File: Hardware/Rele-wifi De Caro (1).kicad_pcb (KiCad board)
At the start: 2 copper layers, 79.3 x 70.1 mm, 38 parts, among them IC1 MC7805CD2TG, J1 Screw_Terminal_01x03, J2 Screw_Terminal_01x03, J3 Screw_Terminal_01x03, J4 Screw_Terminal_01x03, J5 Screw_Terminal_01x02, K1 PR13-5V-450-1C, K2 PR13-5V-450-1C, K3 PR13-5V-450-1C, K4 PR13-5V-450-1C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

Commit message: PCB terminado
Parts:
- moved R3 1.60 mm to (160.3, 75.9)
- moved R2 1.57 mm to (160.2, 63.2)
- moved U2 1.53 mm to (144.0, 70.8)
- moved R1 1.49 mm to (160.2, 70.8)
- moved D1 1.41 mm to (160.2, 67.4), turned to 180 degrees
- moved Q7 0.48 mm to (166.3, 105.9)
- moved 10K4 0.48 mm to (171.1, 109.4)
- moved Q8 0.45 mm to (172.1, 104.4)
- moved IC1 0.44 mm to (140.0, 96.1)
- moved D8 0.43 mm to (171.8, 97.8)
- moved D7 0.40 mm to (161.3, 102.4)
- moved SW1 0.39 mm to (153.6, 96.2)
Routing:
- net VCC: track 177.9 -> 232.2 mm
- net Net-(IC1-VOUT): track 15.8 -> 29.9 mm
- net GPIO 16: track 65.6 -> 69.1 mm
- net Net-(D5-A): track 5.26 -> 6.86 mm
- net Net-(D2-A): track 12.6 -> 11.0 mm
- net Net-(D1-A): track 3.08 -> 4.28 mm
- net Net-(J5-Pin_2): track 16.4 -> 17.4 mm
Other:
- board size 79.3 x 70.1 mm -> 77 x 70.2 mm

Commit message: Add files via upload
PCB terminado
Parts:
- moved J5 56.6 mm to (134.9, 52.8), turned to 90 degrees
- moved SW1 49.1 mm to (145.6, 47.7), turned to 0 degrees
- moved IC1 33.1 mm to (139.6, 63.0)
- moved U2 25.7 mm to (144.0, 96.5)
- moved C5 22.4 mm to (142.1, 70.2)
- moved C6 19.8 mm to (147.8, 70.2), turned to 180 degrees
- moved R3 18.1 mm to (160.2, 94.0)
- moved R1 10.1 mm to (160.2, 80.9)
- moved R4 9.02 mm to (160.2, 99.0), turned to 0 degrees
- moved D5 1.84 mm to (161.2, 85.5), turned to -90 degrees
- moved D1 1.33 mm to (161.2, 68.3), turned to -90 degrees
- moved D7 1.07 mm to (161.2, 103.4), turned to 90 degrees
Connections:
- R1 pad 1: GPIO 15 -> GPIO 2
- R3 pad 1: GPIO 12 -> GPIO 14
- R4 pad 1: GPIO 16 -> GPIO 13
- U2 pad P$15: GPIO 16 -> unconnected-(U2-IO16-PadP$15)
- U2 pad P$3: GPIO 12 -> unconnected-(U2-IO12-PadP$3)
- U2 pad P$4: unconnected-(U2-IO13-PadP$4) -> GPIO 13
- U2 pad P$5: GPIO 15 -> unconnected-(U2-IO15-PadP$5)
- U2 pad P$6: unconnected-(U2-IO14-PadP$6) -> GPIO 14
- U2 pad P$7: unconnected-(U2-IO2-PadP$7) -> GPIO 2
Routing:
- net GPIO 16: track 69.1 -> 0.00 mm
- net VCC: track 232.2 -> 269.9 mm
- net GPIO 4: track 3.78 -> 28.2 mm
- net Net-(IC1-VOUT): track 29.9 -> 48.8 mm
- net GPIO 2: track 0.00 -> 13.5 mm
- net Net-(D1-A): track 4.28 -> 11.7 mm
- net Net-(J5-Pin_2): track 17.4 -> 10.7 mm
- net GPIO 12: track 3.88 -> 0.00 mm
- net GPIO 15: track 3.78 -> 0.00 mm
- net GPIO 13: track 0.00 -> 3.75 mm
- net GPIO 14: track 0.00 -> 3.74 mm
- net Net-(D7-K): track 3.77 -> 6.52 mm
- net Net-(D5-A): track 6.86 -> 7.48 mm
- net (no net): vias 0 -> 2
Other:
- board size 77 x 70.2 mm -> 76.2 x 70.2 mm

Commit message: PCB casi terminado
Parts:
- moved 10K4 0.55 mm to (170.6, 109.4)
- moved Q8 0.55 mm to (171.5, 104.4)
- moved Q7 0.46 mm to (165.8, 105.9)
- moved C5 0.45 mm to (142.5, 70.2), turned to 0 degrees
- moved D8 0.43 mm to (171.3, 97.8)
- moved Q5 0.07 mm to (166.2, 89.1)
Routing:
- net VCC: track 269.9 -> 254.4 mm
- net Net-(D8-A): track 18.0 -> 7.91 mm
- net Net-(D7-K): track 6.52 -> 0.00 mm
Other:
- board size 76.2 x 70.2 mm -> 76.2 x 70.3 mm

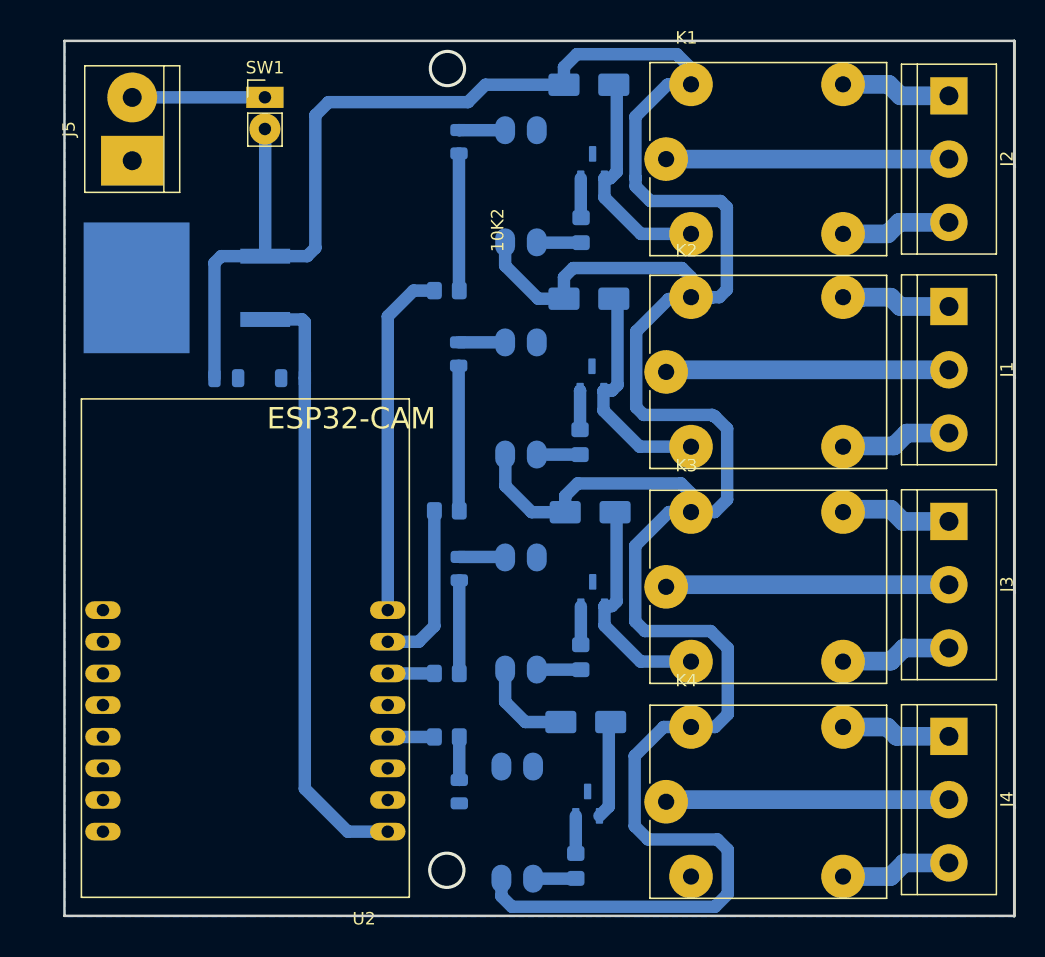
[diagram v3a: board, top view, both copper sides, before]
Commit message: PCB terminado y prolijo
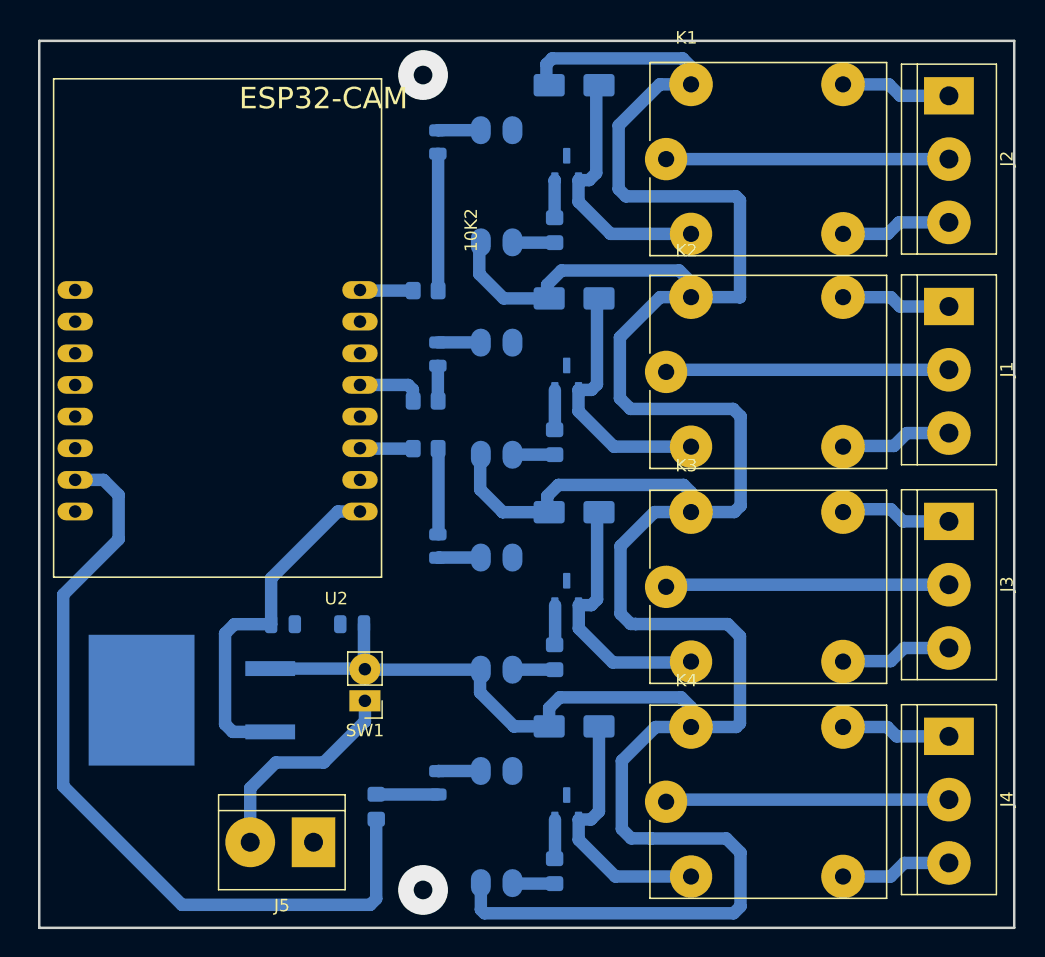
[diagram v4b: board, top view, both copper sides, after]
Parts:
- moved J5 56.6 mm to (149.5, 107.5), turned to 180 degrees
- moved SW1 49.1 mm to (153.6, 96.2), turned to 180 degrees
- moved IC1 33.1 mm to (140.0, 96.1)
- moved U2 25.8 mm to (141.8, 70.8)
- moved C5 22.2 mm to (152.6, 90.0), turned to 180 degrees
- moved C6 19.8 mm to (147.1, 90.0), turned to 0 degrees
- moved R3 18.1 mm to (158.5, 75.9)
- moved R1 8.98 mm to (158.5, 72.1)
- moved R4 7.97 mm to (154.5, 104.6), turned to 90 degrees
- moved D5 2.50 mm to (159.5, 83.7), turned to 90 degrees
- moved 10K2 2.12 mm to (168.8, 58.4)
- moved 10K3 2.10 mm to (168.8, 92.7)
- moved Q6 2.09 mm to (169.8, 87.5)
- moved Q3 2.09 mm to (169.8, 53.4)
- moved 10K1 2.04 mm to (168.8, 75.4)
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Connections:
- R1 pad 1: GPIO 2 -> GPIO 15
- R3 pad 1: GPIO 14 -> GPIO 12
- R4 pad 1: GPIO 13 -> GPIO 16
- U2 pad P$15: unconnected-(U2-IO16-PadP$15) -> GPIO 16
- U2 pad P$3: unconnected-(U2-IO12-PadP$3) -> GPIO 12
- U2 pad P$4: GPIO 13 -> unconnected-(U2-IO13-PadP$4)
- U2 pad P$5: unconnected-(U2-IO15-PadP$5) -> GPIO 15
- U2 pad P$6: GPIO 14 -> unconnected-(U2-IO14-PadP$6)
- U2 pad P$7: GPIO 2 -> unconnected-(U2-IO2-PadP$7)
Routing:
- net GPIO 16: track 0.00 -> 64.9 mm
- net GPIO 4: track 28.2 -> 4.27 mm
- net Net-(IC1-VOUT): track 48.8 -> 28.2 mm
- net GPIO 2: track 13.5 -> 0.00 mm
- net Net-(D8-A): track 7.91 -> 20.6 mm
- net Net-(D1-A): track 11.7 -> 2.83 mm
- net Net-(J5-Pin_2): track 10.7 -> 17.4 mm
- net GPIO 15: track 0.00 -> 5.31 mm
- net GPIO 12: track 0.00 -> 4.28 mm
- net VCC: track 254.4 -> 258.2 mm
- net GPIO 13: track 3.75 -> 0.00 mm
- net GPIO 14: track 3.74 -> 0.00 mm
- net Net-(D7-K): track 0.00 -> 3.42 mm
- net Net-(D6-A): track 18.0 -> 20.7 mm
- net Net-(D3-A): track 18.0 -> 20.5 mm
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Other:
- board size 76.2 x 70.3 mm -> 78.3 x 71.2 mm

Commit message: PCB terminado 2.0
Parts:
- removed Q3, Q4, Q6, Q8: BC547, bc547 smd:SOT95P230X110-3N
- added Q10: BC847, Package_TO_SOT_SMD:SOT-23, B.Cu at (167.5, 104.0)
- added Q11: BC847, Package_TO_SOT_SMD:SOT-23, B.Cu at (167.5, 53.3)
- added Q12: BC847, Package_TO_SOT_SMD:SOT-23, B.Cu at (167.5, 70.0)
- added Q9: BC847, Package_TO_SOT_SMD:SOT-23, B.Cu at (167.5, 87.6)
- added R5: 680, Resistor_SMD:R_0805_2012Metric_Pad1.20x1.40mm_HandSolder, B.Cu at (169.8, 58.6)
- added R6: 680, Resistor_SMD:R_0805_2012Metric_Pad1.20x1.40mm_HandSolder, B.Cu at (169.8, 74.8)
- added R7: 680, Resistor_SMD:R_0805_2012Metric_Pad1.20x1.40mm_HandSolder, B.Cu at (169.8, 92.6)
- added R8: 680, Resistor_SMD:R_0805_2012Metric_Pad1.20x1.40mm_HandSolder, B.Cu at (169.8, 109.8)
- moved D5 17.1 mm to (173.9, 93.0), turned to 180 degrees
- moved D7 16.2 mm to (173.9, 110.3), turned to 180 degrees
- moved D1 16.2 mm to (173.9, 75.8), turned to 180 degrees
- moved D2 16.2 mm to (173.9, 58.7), turned to 180 degrees
- moved R4 3.24 mm to (157.2, 102.8)
- moved R1 2.59 mm to (157.2, 69.8), turned to 90 degrees
- moved 10K1 2.37 mm to (166.5, 74.8)
- moved 10K2 2.31 mm to (166.5, 58.6)
- moved 10K4 2.30 mm to (166.5, 109.8)
- moved 10K3 2.30 mm to (166.5, 92.7)
- moved Q1 2.13 mm to (162.2, 71.3)
- moved Q2 2.06 mm to (162.2, 55.1)
- moved Q5 2.05 mm to (162.2, 89.2)
- moved Q7 2.05 mm to (162.2, 106.3)
- moved R3 1.77 mm to (157.0, 76.8), turned to -90 degrees
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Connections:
- D3 pad 2: Net-(D3-A) -> Net-(D2-K)
- D4 pad 2: Net-(D4-A) -> Net-(D1-K)
- D6 pad 2: Net-(D6-A) -> Net-(D5-K)
- D8 pad 2: Net-(D8-A) -> Net-(D7-K)
- K1 pad A2: Net-(D3-A) -> Net-(D2-K)
- K2 pad A2: Net-(D4-A) -> Net-(D1-K)
- K3 pad A2: Net-(D6-A) -> Net-(D5-K)
- K4 pad A2: Net-(D8-A) -> Net-(D7-K)
- Q1 pad 1: Net-(D1-K) -> Net-(Q1-Pad1)
- Q2 pad 1: Net-(D2-K) -> Net-(Q2-Pad1)
- Q5 pad 1: Net-(D5-K) -> Net-(Q5-Pad1)
- Q7 pad 1: Net-(D7-K) -> Net-(Q7-Pad1)
- R1 pad 2: Net-(D1-A) -> Net-(Q1-Pad1)
- R2 pad 2: Net-(D2-A) -> Net-(Q2-Pad1)
- R3 pad 2: Net-(D5-A) -> Net-(Q5-Pad1)
- R4 pad 1: GPIO 16 -> GPIO 13
- R4 pad 2: Net-(D7-A) -> Net-(Q7-Pad1)
- U2 pad P$15: GPIO 16 -> unconnected-(U2-IO16-PadP$15)
- U2 pad P$4: unconnected-(U2-IO13-PadP$4) -> GPIO 13
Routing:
- net GPIO 13: track 0.00 -> 80.4 mm
- net GPIO 16: track 64.9 -> 0.00 mm
- net Net-(D6-A): track 20.7 -> 0.00 mm
- net Net-(D5-K): track 3.34 -> 24.0 mm
- net Net-(D8-A): track 20.6 -> 0.00 mm
- net Net-(D3-A): track 20.5 -> 0.00 mm
- net Net-(D2-K): track 3.31 -> 23.8 mm
- net Net-(D4-A): track 20.5 -> 0.00 mm
- net Net-(D1-K): track 3.40 -> 21.6 mm
- net Net-(D7-K): track 3.42 -> 21.6 mm
- net Net-(Q2-Pad1): track 0.00 -> 13.7 mm
- net VCC: track 258.2 -> 267.4 mm
- net Net-(Q5-Pad1): track 0.00 -> 8.41 mm
- net Net-(D2-A): track 11.0 -> 3.86 mm
- net Net-(Q1-Pad1): track 0.00 -> 5.27 mm
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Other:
- board size 78.3 x 71.2 mm -> 78.9 x 71.3 mm
